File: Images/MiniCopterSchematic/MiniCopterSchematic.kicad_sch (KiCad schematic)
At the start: 21 parts, among them J1 MPU6050_IMU, M1 MOTOR_DC_1, M2 MOTOR_DC_2, M3 MOTOR_DC_3, M4 MOTOR_DC_4, Q1 FQP20NO6L, Q2 FQP20NO6L, Q3 FQP20NO6L, Q4 FQP20NO6L

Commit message: Add files via upload
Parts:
- renumbered ss1 to A2
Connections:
- net GND: no longer J1.1 (INT)
- net INT: no longer names the net of J1.1 (INT)
- net INT: no longer A1.5 (D2)
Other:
- note added: "Note: The AD0 and INT pins do not need to be connected anywhere. Only connect ADO to GND and INT to D2 (of nano) if issues are encountered."
- note removed: "Note: The AD0 and INT pins do not need to be connected anywhere. Only connect them (as shown above) if issues are encountered."
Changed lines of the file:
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@@
   (title_block
     (title "Mini-Copter")
-    (date "2023-02-23")
-    (rev "2")
+    (date "2023-03-27")
+    (rev "3")
     (comment 4 "By: Ashish Agrahari")
   )
@@
     (stroke (width 0) (type default) (color 0 0 0 0))
   )
-  (wire (pts (xy 63.5 87.63) (xy 68.58 87.63))
-    (stroke (width 0) (type default) (color 0 0 0 0))
-  )
   (wire (pts (xy 241.3 124.46) (xy 243.84 124.46))
     (stroke (width 0) (type default) (color 0 0 0 0))
@@
   )
   (wire (pts (xy 63.5 115.57) (xy 68.58 115.57))
-    (stroke (width 0) (type default) (color 0 0 0 0))
-  )
-  (wire (pts (xy 142.24 127) (xy 144.78 127))
-    (stroke (width 0) (type default) (color 0 0 0 0))
-  )
-  (wire (pts (xy 142.24 124.46) (xy 153.67 124.46))
     (stroke (width 0) (type default) (color 0 0 0 0))
   )
@@
     (effects (font (size 3 3) (thickness 0.6) bold) (justify left bottom))
   )
-  (text "Note: The AD0 and INT pins do not need to be connected anywhere. Only connect them (as shown above) if issues are encountered."
-    (at 25.4 135.89 0)
+  (text "Note: The AD0 and INT pins do not need to be connected anywhere. Only connect ADO to GND and INT to D2 (of nano) if issues are encountered."
+    (at 20.32 135.89 0)
     (effects (font (size 1.27 1.27)) (justify left bottom))
   )
@@
     (effects (font (size 1.27 1.27)) (justify right))
     (property "Intersheet References" "${INTERSHEET_REFS}" (id 0) (at 113.4593 82.4706 0)
-      (effects (font (size 1.27 1.27)) (justify right) hide)
-    )
-  )
-  (global_label "INT" (shape input) (at 63.5 87.63 180) (fields_autoplaced)
-    (effects (font (size 1.27 1.27)) (justify right))
-    (property "Intersheet References" "${INTERSHEET_REFS}" (id 0) (at 58.184 87.5506 0)
       (effects (font (size 1.27 1.27)) (justify right) hide)
     )
@@
     )
   )
-  (global_label "INT" (shape output) (at 144.78 127 0) (fields_autoplaced)
-    (effects (font (size 1.27 1.27)) (justify left))
-    (property "Intersheet References" "${INTERSHEET_REFS}" (id 0) (at 150.096 126.9206 0)
-      (effects (font (size 1.27 1.27)) (justify left) hide)
-    )
-  )
   (global_label "SCL" (shape bidirectional) (at 97.79 113.03 0) (fields_autoplaced)
     (effects (font (size 1.27 1.27)) (justify left))
@@
   (symbol (lib_id "Transistor_FET:IRF540N") (at 39.37 182.88 0) (unit 1)
     (in_bom yes) (on_board yes)
-    (property "Reference" "Q1" (id 0) (at 45.72 181.6099 0)
-      (effects (font (size 1.27 1.27)) (justify left) hide)
+    (property "Reference" "Q1" (id 0) (at 48.26 182.88 0)
+      (effects (font (size 1.27 1.27)) (justify left))
     )
     (property "Value" "FQP20NO6L" (id 1) (at 44.45 185.42 0)
@@
   (symbol (lib_name "Motor_DC_1") (lib_id "Motor:Motor_DC") (at 106.68 175.26 0) (unit 1)
     (in_bom yes) (on_board yes)
-    (property "Reference" "M3" (id 0) (at 93.98 176.5299 0)
-      (effects (font (size 1.27 1.27)) (justify left) hide)
+    (property "Reference" "M3" (id 0) (at 96.52 177.8 0)
+      (effects (font (size 1.27 1.27)) (justify left))
     )
     (property "Value" "MOTOR_DC_3" (id 1) (at 91.44 180.34 0)
@@
   (symbol (lib_name "Motor_DC_1") (lib_id "Motor:Motor_DC") (at 31.75 175.26 0) (unit 1)
     (in_bom yes) (on_board yes)
-    (property "Reference" "M1" (id 0) (at 19.05 176.5299 0)
-      (effects (font (size 1.27 1.27)) (justify left) hide)
+    (property "Reference" "M1" (id 0) (at 21.59 179.07 0)
+      (effects (font (size 1.27 1.27)) (justify left))
     )
     (property "Value" "MOTOR_DC_1" (id 1) (at 17.78 181.61 0)
@@
     (in_bom yes) (on_board yes)
     (property "Reference" "M2" (id 0) (at 57.15 176.5299 0)
-      (effects (font (size 1.27 1.27)) (justify left) hide)
+      (effects (font (size 1.27 1.27)) (justify left))
     )
     (property "Value" "MOTOR_DC_2" (id 1) (at 54.61 180.34 0)
@@
   (symbol (lib_id "Transistor_FET:IRF540N") (at 152.4 182.88 0) (unit 1)
     (in_bom yes) (on_board yes)
-    (property "Reference" "Q4" (id 0) (at 158.75 181.6099 0)
-      (effects (font (size 1.27 1.27)) (justify left) hide)
+    (property "Reference" "Q4" (id 0) (at 161.29 182.88 0)
+      (effects (font (size 1.27 1.27)) (justify left))
     )
     (property "Value" "FQP20NO6L" (id 1) (at 157.48 185.42 0)
@@
   (symbol (lib_id "Transistor_FET:IRF540N") (at 77.47 182.88 0) (unit 1)
     (in_bom yes) (on_board yes)
-    (property "Reference" "Q2" (id 0) (at 83.82 181.6099 0)
-      (effects (font (size 1.27 1.27)) (justify left) hide)
+    (property "Reference" "Q2" (id 0) (at 86.36 182.88 0)
+      (effects (font (size 1.27 1.27)) (justify left))
     )
     (property "Value" "FQP20NO6L" (id 1) (at 82.55 185.42 0)
@@
     (in_bom yes) (on_board yes) (fields_autoplaced)
     (property "Reference" "J1" (id 0) (at 137.16 102.87 0)
-      (effects (font (size 1.143 1.143)) hide)
+      (effects (font (size 1.143 1.143)))
     )
     (property "Value" "MPU6050_IMU" (id 1) (at 137.16 105.41 0)
@@
   )
   (symbol (lib_id "MCU_Module:Arduino_UNO_R3") (at 228.6 124.46 0) (unit 1)
-    (in_bom yes) (on_board yes) (fields_autoplaced)
-    (property "Reference" "ss1" (id 0) (at 235.6994 96.52 0)
-      (effects (font (size 1.27 1.27)) (justify left) hide)
+    (in_bom yes) (on_board yes)
+    (property "Reference" "A2" (id 0) (at 240.03 96.52 0)
+      (effects (font (size 1.27 1.27)) (justify left))
     )
     (property "Value" "ARDUINO_UNO" (id 1) (at 235.6994 99.06 0)
@@
   )
   (symbol (lib_id "MCU_Module:Arduino_Nano_Every") (at 81.28 100.33 0) (unit 1)
-    (in_bom yes) (on_board yes) (fields_autoplaced)
-    (property "Reference" "A1" (id 0) (at 83.2994 125.73 0)
-      (effects (font (size 1.27 1.27)) (justify left) hide)
-    )
-    (property "Value" "ARDUINO NANO EVERY" (id 1) (at 83.2994 125.73 0)
+    (in_bom yes) (on_board yes)
+    (property "Reference" "A1" (id 0) (at 92.71 128.27 0)
+      (effects (font (size 1.27 1.27)) (justify left))
+    )
+    (property "Value" "ARDUINO NANO EVERY" (id 1) (at 83.82 125.73 0)
       (effects (font (size 1.27 1.27)) (justify left))
     )
@@
   (symbol (lib_name "Motor_DC_1") (lib_id "Motor:Motor_DC") (at 144.78 175.26 0) (unit 1)
     (in_bom yes) (on_board yes)
-    (property "Reference" "M4" (id 0) (at 132.08 176.5299 0)
-      (effects (font (size 1.27 1.27)) (justify left) hide)
+    (property "Reference" "M4" (id 0) (at 133.35 177.8 0)
+      (effects (font (size 1.27 1.27)) (justify left))
     )
     (property "Value" "MOTOR_DC_4" (id 1) (at 129.54 180.34 0)
@@
   (symbol (lib_id "Transistor_FET:IRF540N") (at 114.3 182.88 0) (unit 1)
     (in_bom yes) (on_board yes)
-    (property "Reference" "Q3" (id 0) (at 120.65 181.6099 0)
-      (effects (font (size 1.27 1.27)) (justify left) hide)
+    (property "Reference" "Q3" (id 0) (at 123.19 182.88 0)
+      (effects (font (size 1.27 1.27)) (justify left))
     )
     (property "Value" "FQP20NO6L" (id 1) (at 119.38 185.42 0)
@@
     )
     (property "Footprint" "RF_Module:nRF24L01_Breakout" (id 2) (at 214.63 50.8 0)
-      (effects (font (size 1.27 1.27) italic) (justify left) hide)
+      (effects (font (size 1.27 1.27)) (justify left) hide)
     )
     (property "Datasheet" "http://www.nordicsemi.com/eng/content/download/2730/34105/file/nRF24L01_Product_Specification_v2_0.pdf" (id 3) (at 210.82 68.58 0)
@@
     (pin "8")
   )
-  (symbol (lib_id "AA_Custom_Components:GND") (at 153.67 124.46 0) (unit 1)
-    (in_bom yes) (on_board yes) (fields_autoplaced)
-    (property "Reference" "#GND010" (id 0) (at 154.94 125.73 0)
-      (effects (font (size 1.143 1.143)) (justify left bottom) hide)
-    )
-    (property "Value" "GND" (id 1) (at 151.384 130.81 0)
-      (effects (font (size 1.143 1.143)) (justify left bottom) hide)
-    )
-    (property "Footprint" "XXX-00000" (id 2) (at 153.67 121.92 0)
-      (effects (font (size 1.524 1.524)) hide)
-    )
-    (property "Datasheet" "" (id 3) (at 153.67 127 0)
-      (effects (font (size 1.524 1.524)) hide)
-    )
-    (pin "~")
-  )
   (symbol (lib_id "AA_Custom_Components:GND") (at 35.56 78.74 0) (unit 1)
     (in_bom yes) (on_board yes) (fields_autoplaced)
@@
       (reference "#GND09") (unit 1) (value "GND") (footprint "XXX-00000")
     )
-    (path "/f0f718e6-16a1-495d-9d9e-2de6d83ac0c4"
-      (reference "#GND010") (unit 1) (value "GND") (footprint "XXX-00000")
-    )
     (path "/6d5d5132-1a78-4b19-839b-13f51792e79c"
       (reference "#GND011") (unit 1) (value "GND") (footprint "XXX-00000")
@@
       (reference "A1") (unit 1) (value "ARDUINO NANO EVERY") (footprint "Module:Arduino_Nano")
     )
+    (path "/85446842-eaf6-4de0-8544-0fc7808b3ec9"
+      (reference "A2") (unit 1) (value "ARDUINO_UNO") (footprint "Module:Arduino_UNO_R3")
+    )
     (path "/70fbff7a-f0df-40b1-9155-b6abad2a2d0f"
       (reference "J1") (unit 1) (value "MPU6050_IMU") (footprint "")
@@
       (reference "R4") (unit 1) (value "10K Ω") (footprint "")
     )
-    (path "/85446842-eaf6-4de0-8544-0fc7808b3ec9"
-      (reference "ss1") (unit 1) (value "ARDUINO_UNO") (footprint "Module:Arduino_UNO_R3")
-    )
-  )
+  )

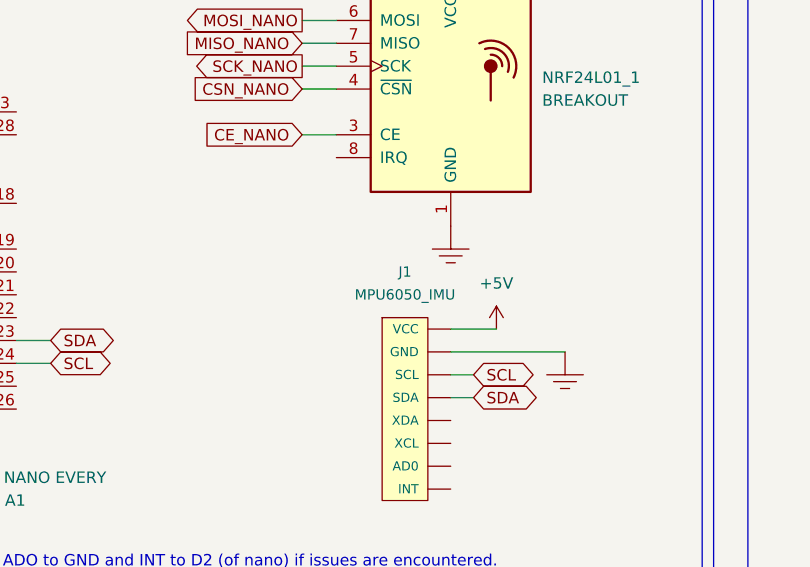
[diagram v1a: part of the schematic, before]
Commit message: Assigned footprints to symbols
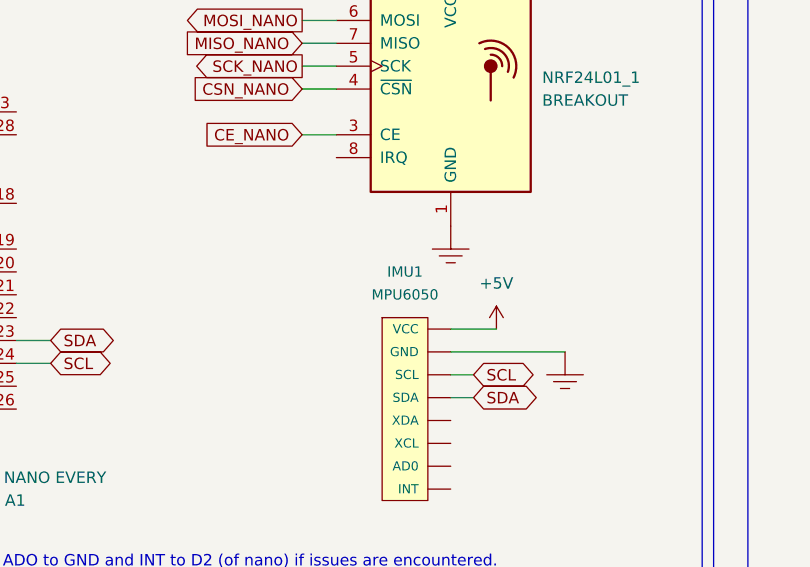
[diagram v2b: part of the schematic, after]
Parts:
- IMU1: renamed from J1; value MPU6050_IMU -> MPU6050; footprint (none) -> Connector_PinSocket_2.54mm:PinSocket_1x07_P2.54mm_Vertical
- LIPO_BATTERY_1, LIPO_BATTERY_2: footprint (none) -> AA_Custom_Components:PowerPad_Pair_5.0x5.0mm
- M1, M2, M3, M4: footprint (none) -> AA_Custom_Components:PowerPad_Pair_4.0x4.0mm
- NRF24L01_1, NRF24L01_2: footprint RF_Module:nRF24L01_Breakout -> AA_Custom_Components:NRF24L01_Breakout
- Q1, Q2, Q3, Q4: footprint Package_TO_SOT_THT:TO-220-3_Vertical -> Connector_PinSocket_2.54mm:PinSocket_1x03_P2.54mm_Vertical
- R1, R2, R3, R4: footprint (none) -> Resistor_THT:R_Axial_DIN0207_L6.3mm_D2.5mm_P10.16mm_Horizontal
